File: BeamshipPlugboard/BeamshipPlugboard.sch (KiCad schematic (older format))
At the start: 4 parts, among them J1 BEAMSPRING PLUGBOARD COLUMNS, J2 BEAMSPRING PLUGBOARD ROWS, J7 Conn_01x34

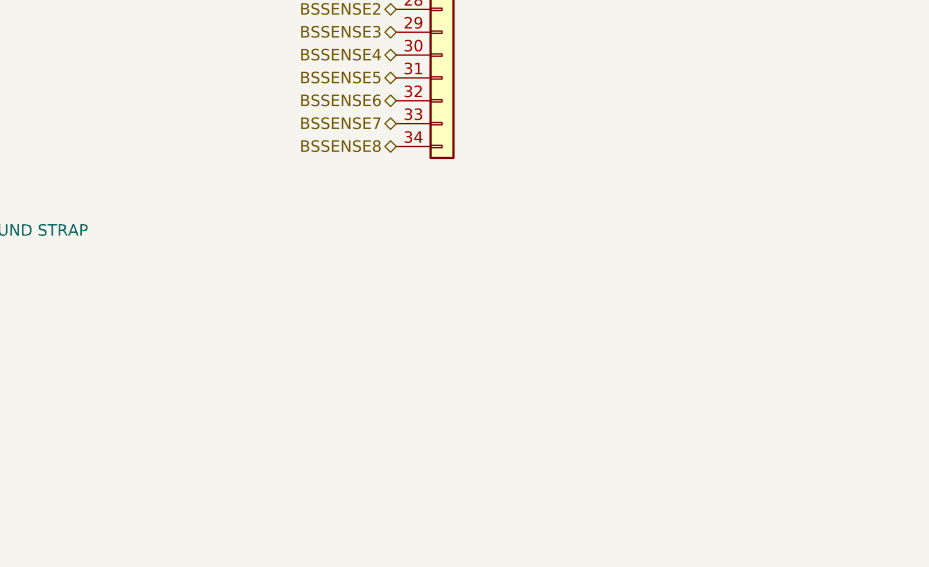
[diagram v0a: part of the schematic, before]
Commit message: Various changes to revision 0.1.1
General:
    Made mounting hole bigger (M3). And moved it a little bit so it doesn't interfere with some components.
    Star ground turned into single ground.
    Ground fills added everywhere.
    Many stitching vias added everywhere.
    Added JLCJLCJLCJLC magic string under pro micro. When ordering from JLCPCB, you can select for Order Number: "Specify Location"
    Bumped version number to 0.1.1
    Added silkscreen to mark rows/columns everywhere.
    Added optional holes for soldering grounding wires everywhere.
Controller:
    Added silkscreen to ease debugging, by marking various important nets.
    Rearranged some traces to maintain better separation between traces, and better ground reference.
Model F plugboard:
    Modified 3.96mm pitch holes, to hole sizes and pad sizes that match original xwhatsit model F controller
    Moved 3.96mm pitch holes closer to the edge, so it doesn't interfere with case in F AT cases.
    Added mounting holes
    Added holes to support 3178 keyboards.
Displaywriter:
    Addes support for more connector types. (The displaywriter daughterboard is now taller)
Beamspring:
    Bugfix to a mistake that only affected people that ran update footprints from library.
Beamship daughterboard:
    Added support for more connectors. Added breakoff-able mounting hole.
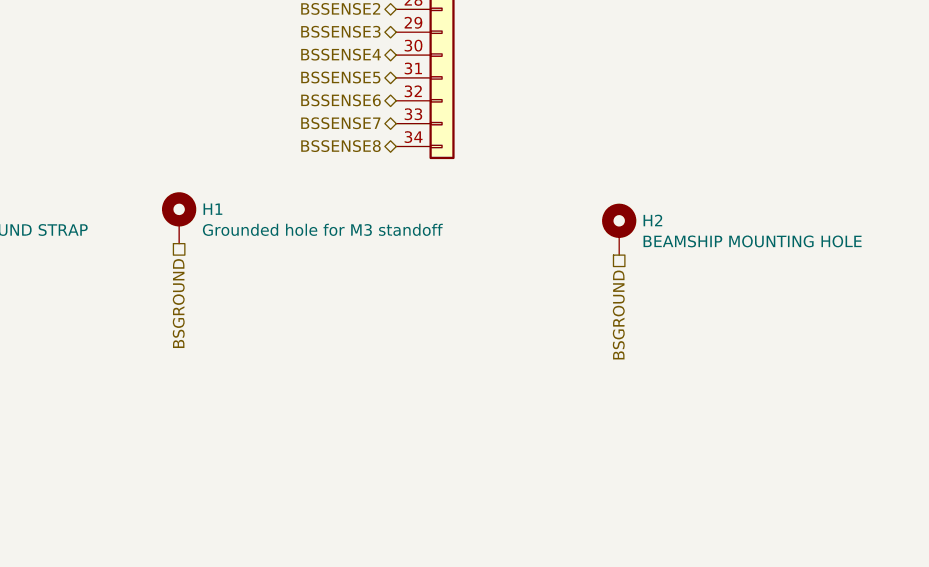
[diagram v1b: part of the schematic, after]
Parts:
- added H1: Grounded hole for M3 standoff, MountingHole:MountingHole_3.2mm_M3_Pad_Via, symbol Mechanical:MountingHole_Pad
- added H2: BEAMSHIP MOUNTING HOLE, TH-XWhatsIt:beamship_mounting_hole, symbol Mechanical:MountingHole_Pad
- J7: footprint TH-XWhatsIt:beamship_new -> TH-XWhatsIt:beamship_new_2
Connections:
- net BSGROUND: now also H1.1, H2.1
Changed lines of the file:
@@
 F 0 "J7" H 7430 2642 50  0000 L CNN
 F 1 "Conn_01x34" H 7430 2551 50  0000 L CNN
-F 2 "TH-XWhatsIt:beamship_new" H 7350 2650 50  0001 C CNN
+F 2 "TH-XWhatsIt:beamship_new_2" H 7350 2650 50  0001 C CNN
 F 3 "~" H 7350 2650 50  0001 C CNN
 	1    7350 2650
@@
 Text HLabel 7150 4350 0    50   BiDi ~ 0
 BSSENSE8
+$Comp
+L Mechanical:MountingHole_Pad H1
+U 1 1 5F9ED074
+P 6200 4675
+F 0 "H1" H 6300 4724 50  0000 L CNN
+F 1 "Grounded hole for M3 standoff" H 6300 4633 50  0000 L CNN
+F 2 "MountingHole:MountingHole_3.2mm_M3_Pad_Via" H 6200 4675 50  0001 C CNN
+F 3 "~" H 6200 4675 50  0001 C CNN
+	1    6200 4675
+	1    0    0    -1
+$EndComp
+Text HLabel 6200 4775 3    50   UnSpc ~ 0
+BSGROUND
+$Comp
+L Mechanical:MountingHole_Pad H2
+U 1 1 5F9EA590
+P 8125 4725
+F 0 "H2" H 8225 4774 50  0000 L CNN
+F 1 "BEAMSHIP MOUNTING HOLE" H 8225 4683 50  0000 L CNN
+F 2 "TH-XWhatsIt:beamship_mounting_hole" H 8125 4725 50  0001 C CNN
+F 3 "~" H 8125 4725 50  0001 C CNN
+	1    8125 4725
+	1    0    0    -1
+$EndComp
+Text HLabel 8125 4825 3    50   UnSpc ~ 0
+BSGROUND
 $EndSCHEMATC

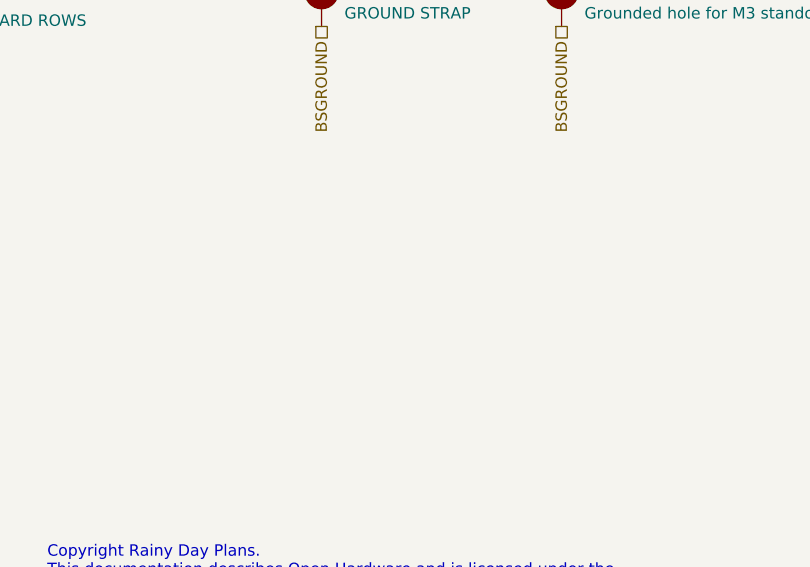
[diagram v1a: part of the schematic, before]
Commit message: Beamship Plugboard: added extra grounding hole.
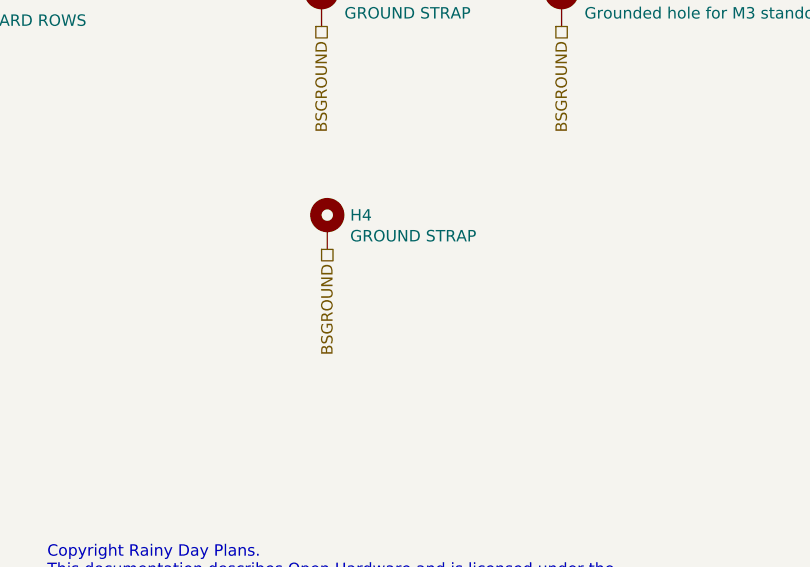
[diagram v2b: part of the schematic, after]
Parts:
- added H4: GROUND STRAP, TH-XWhatsIt:ChassisGnd, symbol Mechanical:MountingHole_Pad
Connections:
- net BSGROUND: now also H4.1
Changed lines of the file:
@@
 Text HLabel 8125 4825 3    50   UnSpc ~ 0
 BSGROUND
+$Comp
+L Mechanical:MountingHole_Pad H4
+U 1 1 600FC64C
+P 5175 5650
+F 0 "H4" H 5275 5699 50  0000 L CNN
+F 1 "GROUND STRAP" H 5275 5608 50  0000 L CNN
+F 2 "TH-XWhatsIt:ChassisGnd" H 5175 5650 50  0001 C CNN
+F 3 "~" H 5175 5650 50  0001 C CNN
+	1    5175 5650
+	1    0    0    -1
+$EndComp
+Text HLabel 5175 5750 3    50   UnSpc ~ 0
+BSGROUND
 $EndSCHEMATC
